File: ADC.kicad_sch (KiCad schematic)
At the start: 4 parts, among them Q1 IRLML6402TRPBF, U3 IRLML2502TRPBF

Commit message: inital layout of components complete
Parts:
- renumbered R13 to R12, R14 to R13
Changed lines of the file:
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@@
   (symbol (lib_id "Device:R_US") (at 135.89 85.09 0) (unit 1)
     (in_bom yes) (on_board yes) (dnp no) (fields_autoplaced)
-    (property "Reference" "R13" (at 138.43 83.82 0)
+    (property "Reference" "R12" (at 138.43 83.82 0)
       (effects (font (size 1.27 1.27)) (justify left))
     )
@@
       (project "key-fob-pcb"
         (path "/b002c3bf-fc58-4993-80f7-7914d3aa1ac9/793a15b3-1bcd-4264-9b18-9575705590fa"
-          (reference "R13") (unit 1)
+          (reference "R12") (unit 1)
         )
       )
@@
   (symbol (lib_id "Device:R_US") (at 163.83 107.95 0) (unit 1)
     (in_bom yes) (on_board yes) (dnp no) (fields_autoplaced)
-    (property "Reference" "R14" (at 166.37 106.68 0)
+    (property "Reference" "R13" (at 166.37 106.68 0)
       (effects (font (size 1.27 1.27)) (justify left))
     )
@@
       (project "key-fob-pcb"
         (path "/b002c3bf-fc58-4993-80f7-7914d3aa1ac9/793a15b3-1bcd-4264-9b18-9575705590fa"
-          (reference "R14") (unit 1)
+          (reference "R13") (unit 1)
         )
       )

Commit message: generate fab files
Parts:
- Q1: MPN (none) -> C2593
- R12, R13: MPN (none) -> C5369222
- U3: MPN (none) -> C2589
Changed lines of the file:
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@@
       (effects (font (size 1.27 1.27)) (justify bottom) hide)
+    )
+    (property "MPN" "C2593" (at 163.83 93.98 0)
+      (effects (font (size 1.27 1.27)) hide)
     )
     (pin "1")
@@
     )
     (property "Datasheet" "" (at 133.35 106.68 0)
+      (effects (font (size 1.27 1.27)) hide)
+    )
+    (property "MPN" "C2589" (at 133.35 106.68 0)
       (effects (font (size 1.27 1.27)) hide)
     )
@@
       (effects (font (size 1.27 1.27)) hide)
     )
+    (property "MPN" "C5369222" (at 135.89 85.09 0)
+      (effects (font (size 1.27 1.27)) hide)
+    )
     (pin "1")
     (pin "2")
@@
       (effects (font (size 1.27 1.27)) hide)
     )
+    (property "MPN" "C5369222" (at 163.83 107.95 0)
+      (effects (font (size 1.27 1.27)) hide)
+    )

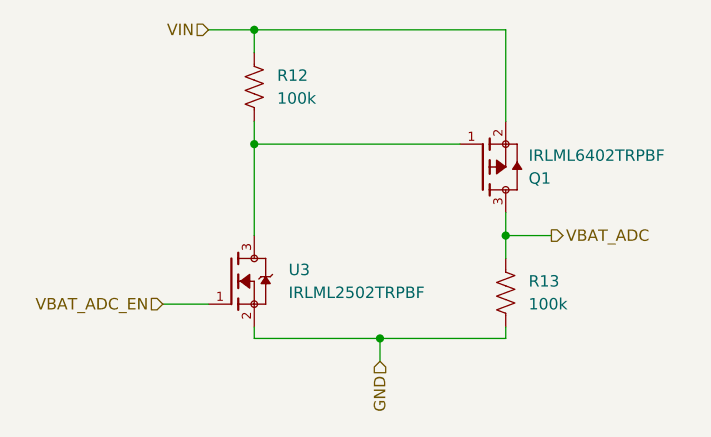
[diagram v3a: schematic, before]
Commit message: replace GND heriarchical labels with GND symbols
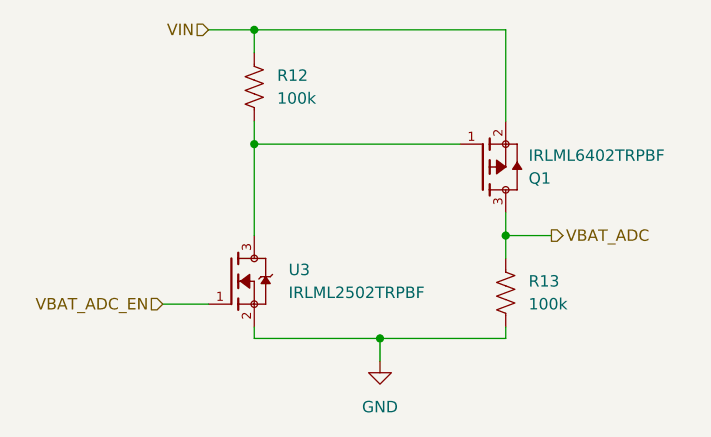
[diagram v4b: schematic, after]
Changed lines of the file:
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@@
     (stroke (width 0) (type default))
-  )
-  (hierarchical_label "GND" (shape input) (at 149.86 115.57 270) (fields_autoplaced)
-    (effects (font (size 1.27 1.27)) (justify right))
   )
   (hierarchical_label "VIN" (shape input) (at 130.81 78.74 180) (fields_autoplaced)
@@
     (effects (font (size 1.27 1.27)) (justify left))
   )
+  (symbol (lib_id "power:GND") (at 149.86 115.57 0) (unit 1)
+    (in_bom yes) (on_board yes) (dnp no) (fields_autoplaced)
+    (property "Reference" "#PWR02" (at 149.86 121.92 0)
+      (effects (font (size 1.27 1.27)) hide)
+    )
+    (property "Value" "GND" (at 149.86 120.65 0)
+      (effects (font (size 1.27 1.27)))
+    )
+    (property "Footprint" "" (at 149.86 115.57 0)
+      (effects (font (size 1.27 1.27)) hide)
+    )
+    (property "Datasheet" "" (at 149.86 115.57 0)
+      (effects (font (size 1.27 1.27)) hide)
+    )
+    (pin "1")
+    (instances
+      (project "key-fob-pcb"
+        (path "/b002c3bf-fc58-4993-80f7-7914d3aa1ac9/97ab50b4-0765-4242-8cdd-feb1ed8d7056"
+          (reference "#PWR02") (unit 1)
+        )
+        (path "/b002c3bf-fc58-4993-80f7-7914d3aa1ac9/793a15b3-1bcd-4264-9b18-9575705590fa"
+          (reference "#PWR09") (unit 1)
+        )
+      )
+    )
+  )
   (symbol (lib_id "IRLML6402TRPBF:IRLML6402TRPBF") (at 163.83 93.98 0) (mirror x) (unit 1)

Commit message: add author to each sheet
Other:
- company: (none) -> J2B
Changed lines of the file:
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@@
   (title_block
     (title "Key Fob")
-    (date "2023-10-31")
+    (date "2023-10-17")
+    (company "J2B")
+    (comment 1 "Author: Ben Martens")
   )
   (junction (at 135.89 91.44) (diameter 0) (color 0 0 0 0)
